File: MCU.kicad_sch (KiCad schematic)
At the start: 52 parts, among them IC1 MT2492, J1 FH34SRJ-8S-0.5SH_50_, U1 TEENSY 4.0, U2 ESP32-C3-MINI-1-H4X, U3 TLV75733PDBV

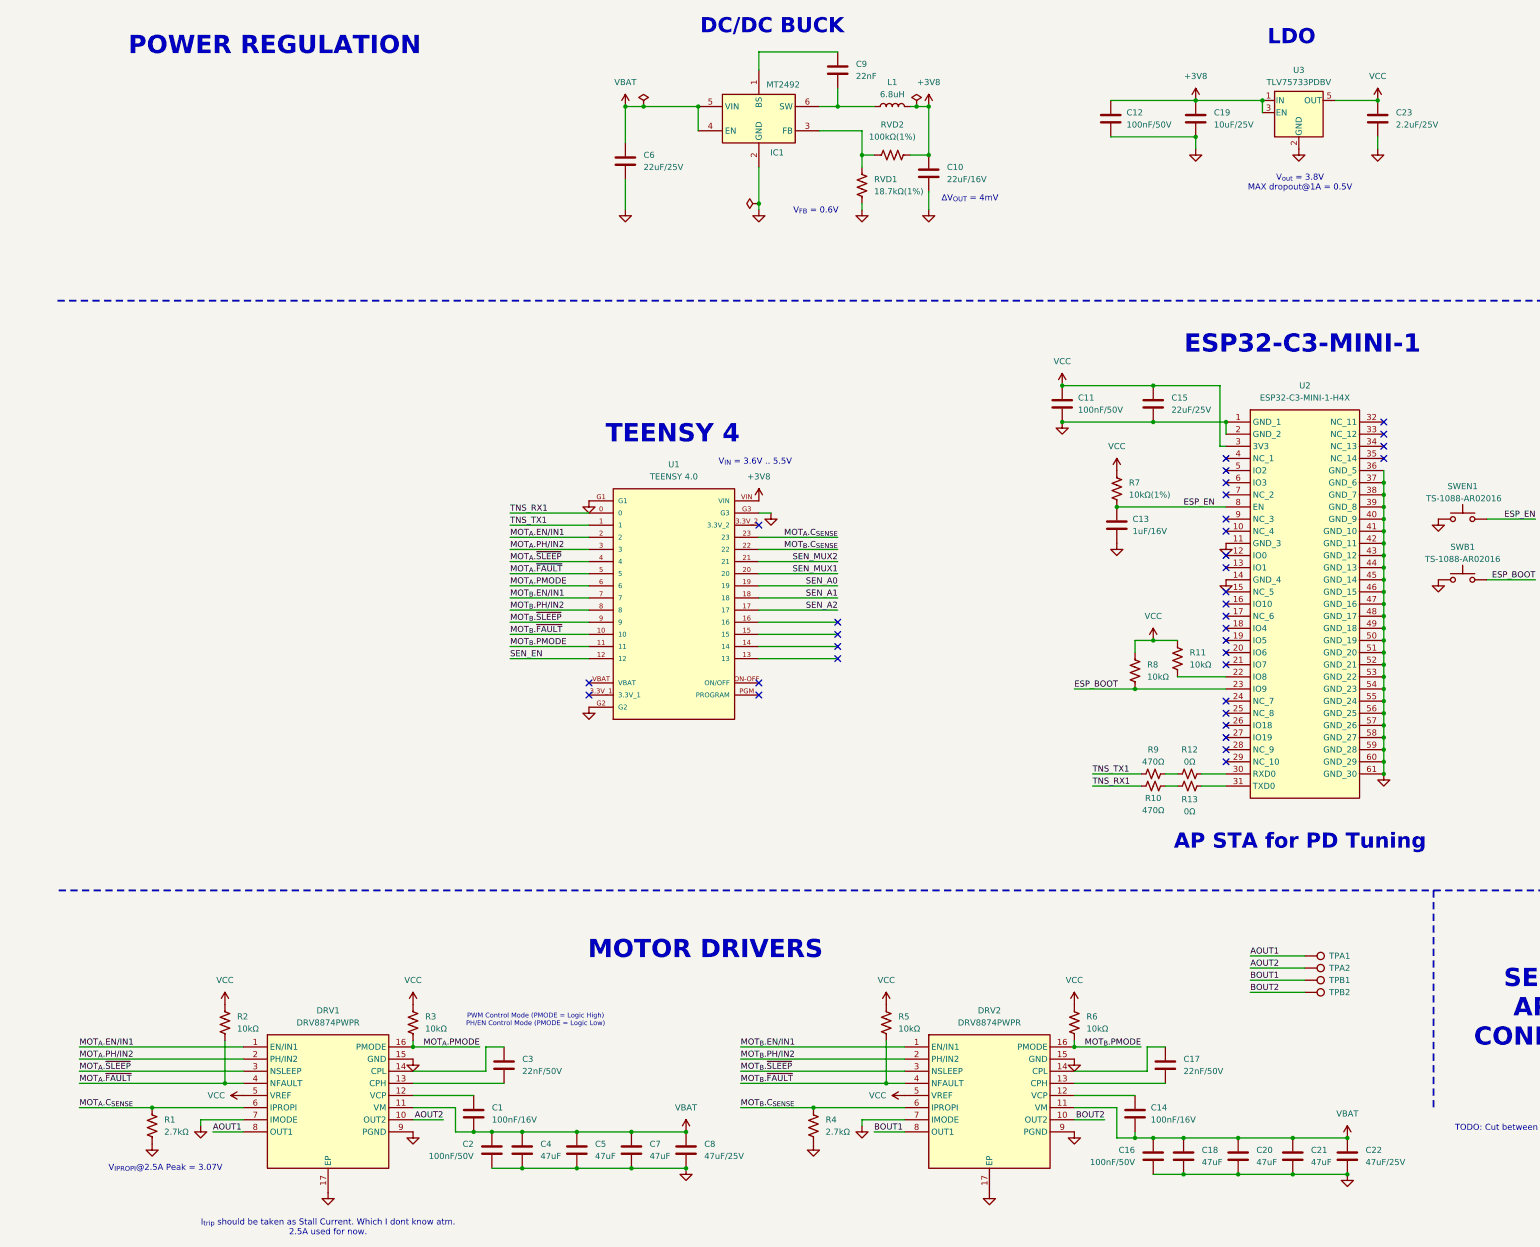
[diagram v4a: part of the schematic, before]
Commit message: Added dedicated Current Sensing IC INA240. Changed Buck output from 3.8V (edge of Teensy's LDO supply voltage) to 5V.
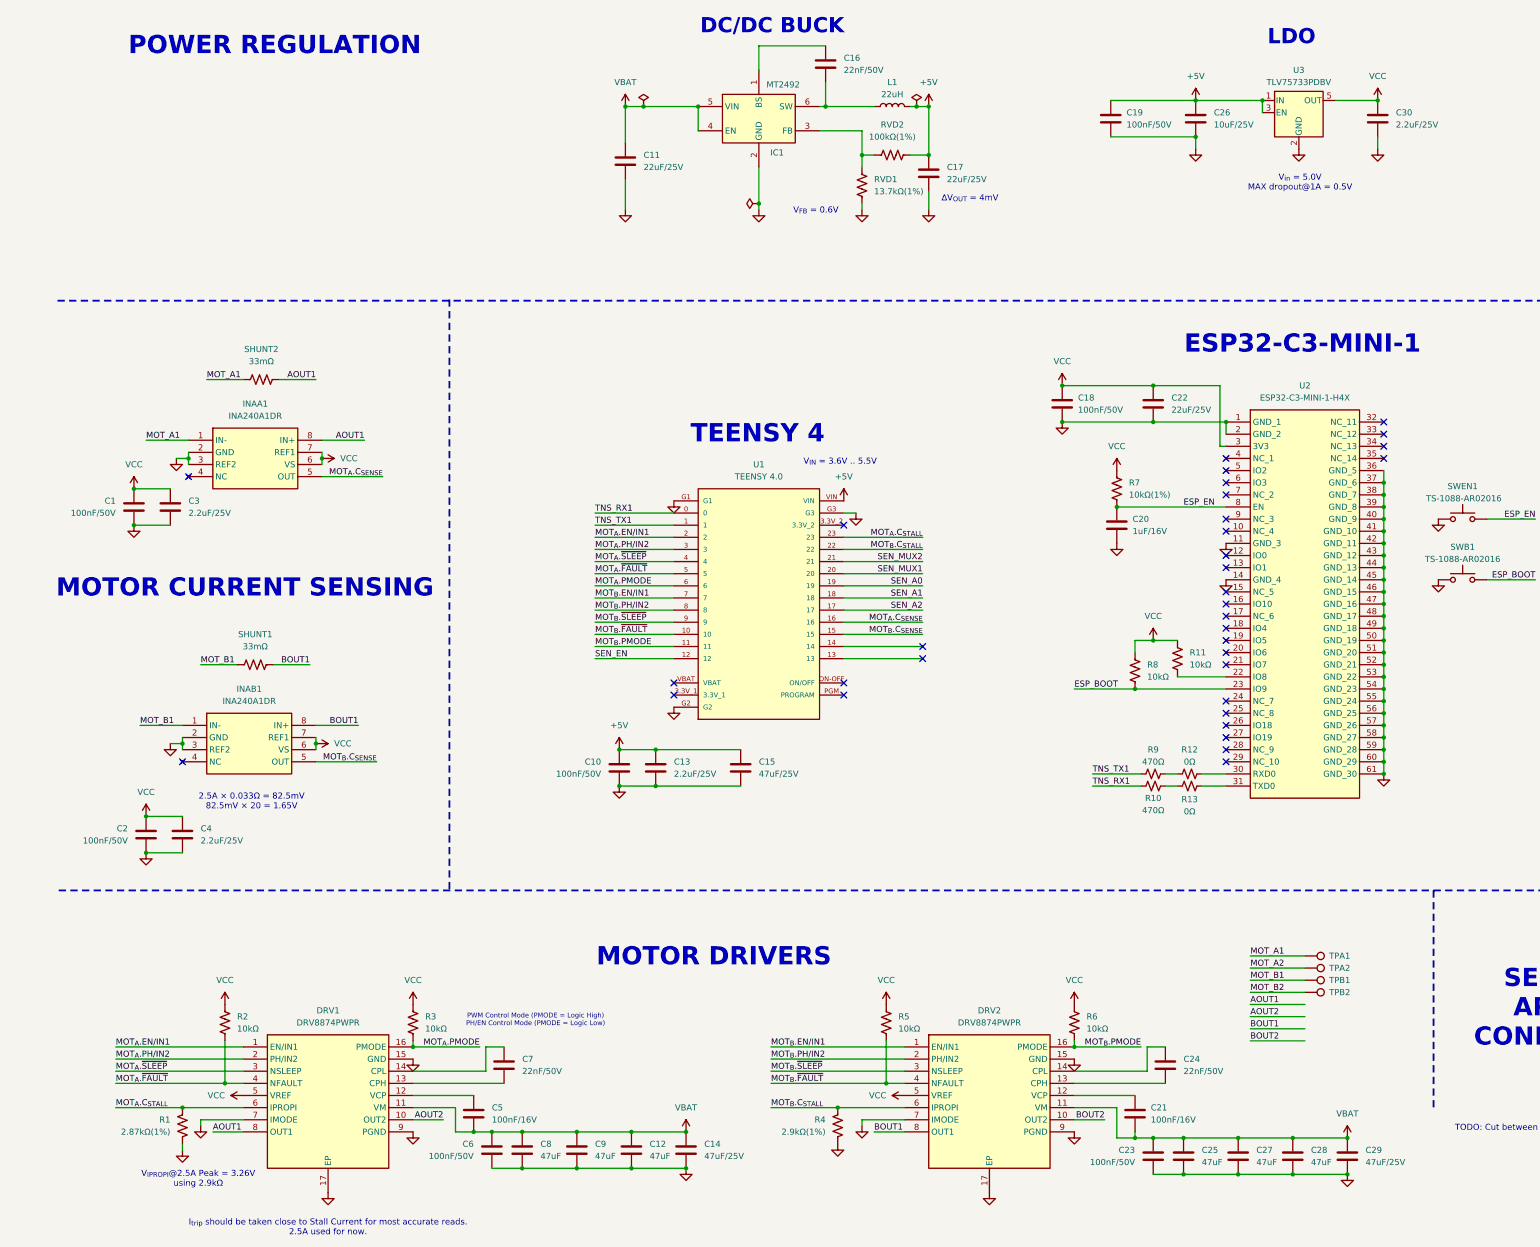
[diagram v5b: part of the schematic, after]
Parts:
- added C1, C10, C2: 100nF/50V, symbol Device:C
- added C13, C3, C4: 2.2uF/25V, symbol Device:C
- added C15: 47uF/25V, Capacitor_SMD:C_1206_3216Metric_Pad1.33x1.80mm_HandSolder, symbol Device:C
- added INAA1, INAB1: INA240A1DR, SAVITAR:SOIC127P600X175-8N, symbol SAVITAR:INA240A1DR
- added SHUNT1, SHUNT2: 33mΩ, symbol Device:R_US
- C16: renamed from C9; value 22nF -> 22nF/50V
- C17: renamed from C10; value 22uF/16V -> 22uF/25V
- L1: value 6.8uH -> 22uH; footprint Inductor_SMD:L_1210_3225Metric_Pad1.42x2.65mm_HandSolder -> Inductor_SMD:L_1210_3225Metric
- R1: value 2.7kΩ -> 2.87kΩ(1%)
- R4: value 2.7kΩ -> 2.9kΩ(1%)
- RVD1: value 18.7kΩ(1%) -> 13.7kΩ(1%)
- renumbered C6 to C11, C7 to C12, C8 to C14, C11 to C18, C12 to C19, C13 to C20, C14 to C21, C15 to C22, C16 to C23, C17 to C24, C18 to C25, C19 to C26, C20 to C27, C21 to C28, C22 to C29, C23 to C30, C1 to C5, C2 to C6, C3 to C7, C4 to C8, C5 to C9
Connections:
- net AOUT1: now also INAA1.8 (IN+), SHUNT2.2; no longer TPA1.1
- net AOUT2: no longer TPA2.1
- net BOUT1: now also INAB1.8 (IN+), SHUNT1.2; no longer TPB1.1
- net BOUT2: no longer TPB2.1
- net GND: now also C1.1, C10.1, C13.1, C15.2, C2.1, C3.1, C4.1, INAA1.2 (GND), INAA1.3 (REF2), INAB1.2 (GND), INAB1.3 (REF2)
- net MOT_{A}.C_{SENSE}: now also U1.16, INAA1.5 (OUT); no longer DRV1.6 (IPROPI), R1.1, U1.23
- net MOT_{B}.C_{SENSE}: now also U1.15, INAB1.5 (OUT); no longer DRV2.6 (IPROPI), R4.1, U1.22
- net VCC: now also C1.2, C2.2, C3.2, C4.2, INAA1.6 (VS), INAA1.7 (REF1), INAB1.6 (VS), INAB1.7 (REF1)
- net +3V8 renamed +5V
- net +5V: now also C10.2, C13.2, C15.1
- new net MOT_A1: INAA1.1 (IN-), SHUNT2.1, TPA1.1
- new net MOT_A2: TPA2.1
- new net MOT_B1: INAB1.1 (IN-), SHUNT1.1, TPB1.1
- new net MOT_B2: TPB2.1
- new net MOT_{A}.C_{STALL}: DRV1.6 (IPROPI), R1.1, U1.23
- new net MOT_{B}.C_{STALL}: DRV2.6 (IPROPI), R4.1, U1.22
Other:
- note added: "2.5A × 0.033Ω = 82.5mV 82.5mV × 20 = 1.65V"
- note added: "I_{trip} should be taken close to Stall Current for most accurate reads. 2.5A used for now."
- note added: "MOTOR CURRENT SENSING"
- note added: "V_{IPROPI}@2.5A Peak = 3.26V using 2.9kΩ"
- note added: "V_{in} = 5.0V MAX dropout@1A = 0.5V"
- note removed: "AP STA for PD Tuning"
- note removed: "I_{trip} should be taken as Stall Current. Which I dont know atm. 2.5A used for now."
- note removed: "V_{IPROPI}@2.5A Peak = 3.07V"
- note removed: "V_{out} = 3.8V MAX dropout@1A = 0.5V"
- title: TEENSY 4 MCU -> TEENSY 4 ESP32 MCU
- moved on the sheet: C16, R1, R4, U1

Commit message: Added decoupling for sensor board. Changed the relatively old CD4051BM with over 400 ohm to 74HC4051. Added for the first time hierarchical label to connect the FFC pins across schematics.
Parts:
- added D1, D2: SML-D12D8WT86, LED_SMD:LED_0603_1608Metric, symbol Device:LED
- added R18, R19: 510Ω, Resistor_SMD:R_0603_1608Metric, symbol Device:R_US
- added R4: 100kΩ(1%), Resistor_SMD:R_0603_1608Metric, symbol Device:R_US
- added R5: 33kΩ(1%), Resistor_SMD:R_0603_1608Metric, symbol Device:R_US
- C1, C10, C13, C16, C18, C19, C2, C20, C21, C23, C24, C26, C3, C30, C4, C5, C6, C7: footprint (none) -> Capacitor_SMD:C_0603_1608Metric
- C11: renamed from C12; footprint Capacitor_SMD:C_1206_3216Metric_Pad1.33x1.80mm_HandSolder -> Capacitor_SMD:C_1206_3216Metric
- C12: renamed from C11; footprint (none) -> Capacitor_SMD:C_0805_2012Metric
- C14, C15, C22, C25, C27, C28, C29, C8, C9: footprint Capacitor_SMD:C_1206_3216Metric_Pad1.33x1.80mm_HandSolder -> Capacitor_SMD:C_1206_3216Metric
- C17: footprint (none) -> LED_SMD:LED_0805_2012Metric
- R1, R2, R3: footprint (none) -> Resistor_SMD:R_0603_1608Metric
- R10: renamed from R6; footprint (none) -> Resistor_SMD:R_0603_1608Metric
- R11: renamed from R7; footprint (none) -> Resistor_SMD:R_0603_1608Metric
- R12: renamed from R8; footprint (none) -> Resistor_SMD:R_0603_1608Metric
- R13: renamed from R9; footprint (none) -> Resistor_SMD:R_0603_1608Metric
- R14: renamed from R10; footprint (none) -> Resistor_SMD:R_0603_1608Metric
- R15: renamed from R11; footprint (none) -> Resistor_SMD:R_0603_1608Metric
- R16: renamed from R12; footprint (none) -> Resistor_SMD:R_0603_1608Metric
- R17: renamed from R13; footprint (none) -> Resistor_SMD:R_0603_1608Metric
- R6: renamed from R4; value 2.9kΩ(1%) -> 2.87kΩ(1%); footprint (none) -> Resistor_SMD:R_0603_1608Metric
- R7: renamed from RVD1; footprint (none) -> Resistor_SMD:R_0603_1608Metric
- R8: renamed from R5; footprint (none) -> Resistor_SMD:R_0603_1608Metric
- R9: renamed from RVD2; footprint (none) -> Resistor_SMD:R_0603_1608Metric
- SHUNT1, SHUNT2: footprint (none) -> Resistor_SMD:R_1206_3216Metric
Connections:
- net AOUT2 is gone; now on net MOT_A2: DRV1.10 (OUT2)
- net BOUT2 is gone; now on net MOT_B2: DRV2.10 (OUT2)
- net GND: now also D1.1 (K), D2.1 (K), R5.1
- net VBAT: now also R4.2
- net STATUS_LED: now reaches U1.13
- net STATUS_LED: now also R18.1, R19.1
- net BAT_LEVEL: now reaches U1.14
- net BAT_LEVEL: now also R4.1, R5.2
- net AOUT1 renamed SENSE_IN_A1
- net BOUT1 renamed SENSE_IN_B1
- net MOT_{A}.C_{SENSE} renamed MOT_A.C_SENSE
- net MOT_{A}.C_{STALL} renamed MOT_A.C_STALL
- net MOT_{A}.EN/IN1 renamed MOT_A.EN/IN1
- net MOT_{A}.PH/IN2 renamed MOT_A.PH/IN2
- net MOT_{A}.PMODE renamed MOT_A.PMODE
- net MOT_{A}.~{FAULT} renamed MOT_A.~{FAULT}
- net MOT_{A}.~{SLEEP} renamed MOT_A.~{SLEEP}
- net MOT_{B}.C_{SENSE} renamed MOT_B.C_SENSE
- net MOT_{B}.C_{STALL} renamed MOT_B.C_STALL
- net MOT_{B}.EN/IN1 renamed MOT_B.EN/IN1
- net MOT_{B}.PH/IN2 renamed MOT_B.PH/IN2
- net MOT_{B}.PMODE renamed MOT_B.PMODE
- net MOT_{B}.~{FAULT} renamed MOT_B.~{FAULT}
- net MOT_{B}.~{SLEEP} renamed MOT_B.~{SLEEP}
- net SEN_A0 renamed A0
- net SEN_A1 renamed A1
- net SEN_A2 renamed A2
- net SEN_EN renamed EN
- net SEN_MUX1 renamed MUX1
- net SEN_MUX2 renamed MUX2
- new net: D1.2 (A), R18.2
- new net: D2.2 (A), R19.2
- no-connect marks 34 -> 32
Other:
- note added: "STATUS LED"
- moved on the sheet: C10, C12, C13, C15, R1, R6, SWB1, SWEN1, TPA1, TPA2, TPB1, TPB2
